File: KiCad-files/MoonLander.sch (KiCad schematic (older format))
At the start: 6 parts, among them P1 CONN_01X02, P2 CONN_01X02, P3 USB_OTG

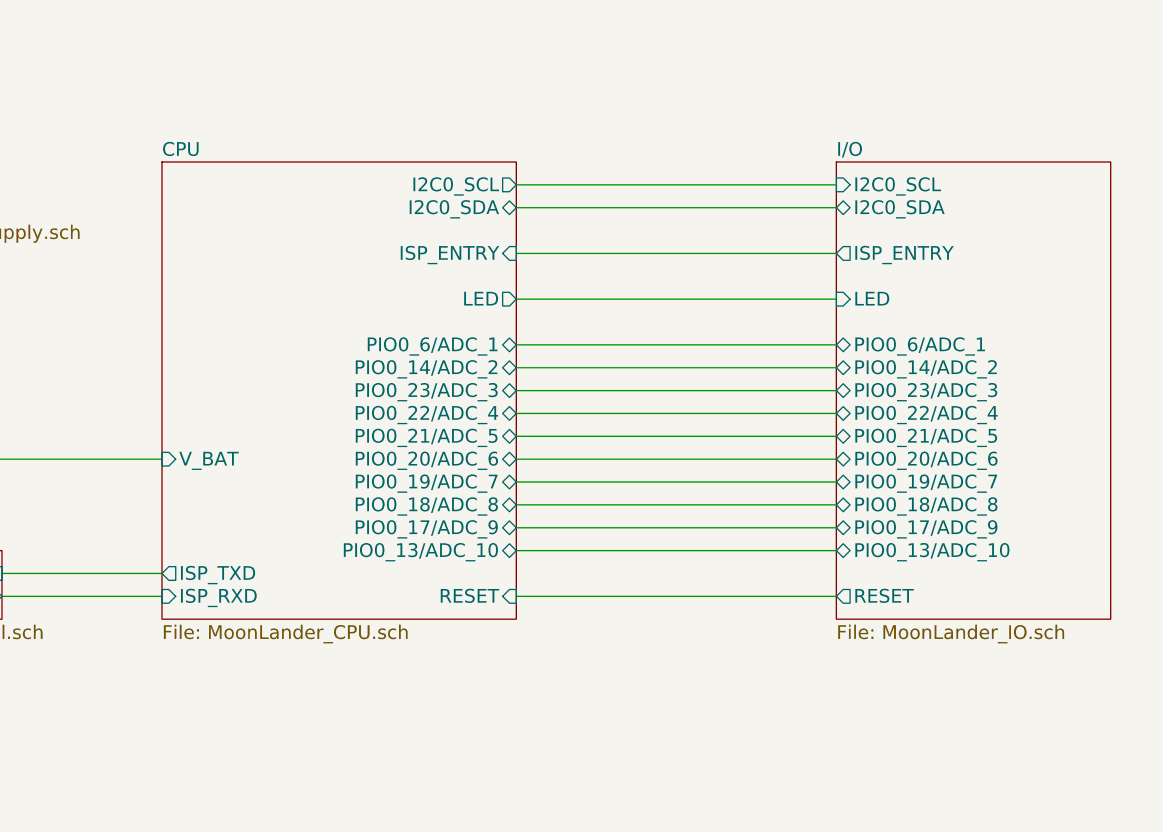
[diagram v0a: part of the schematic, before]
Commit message: added I2C EEPROM, redid ground stitching
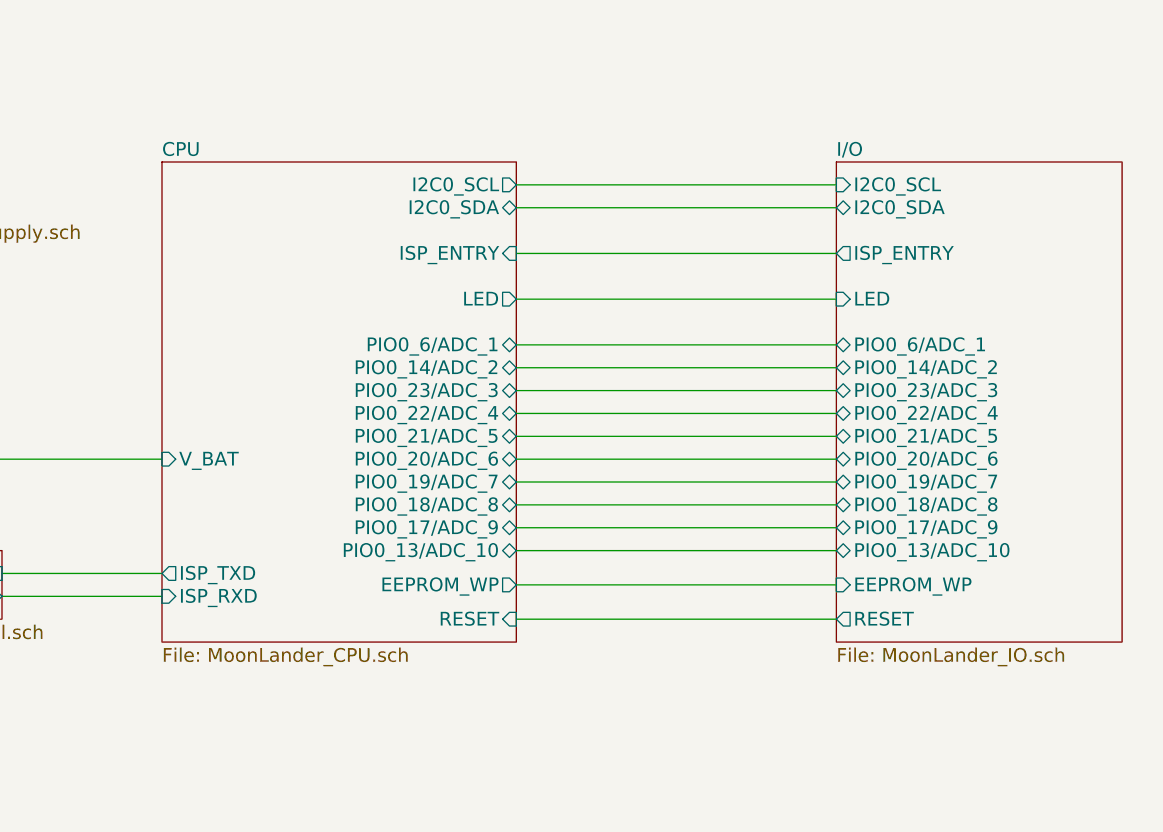
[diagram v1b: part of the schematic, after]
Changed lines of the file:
@@
 5V DC external supply
 $Sheet
-S 8450 2550 1200 2000
+S 8450 2550 1250 2100
 U 566094B7
 F0 "I/O" 60
@@
 F13 "PIO0_22/ADC_4" B L 8450 3650 60
 F14 "PIO0_23/ADC_3" B L 8450 3550 60
-F15 "RESET" O L 8450 4450 60
+F15 "RESET" O L 8450 4550 60
 F16 "LED" I L 8450 3150 60
+F17 "EEPROM_WP" I L 8450 4400 60
 $EndSheet
 Wire Wire Line
@@
 Connection ~ 3400 2700
 $Sheet
-S 5500 2550 1550 2000
+S 5500 2550 1550 2100
 U 565F2D6A
 F0 "CPU" 60
@@
 F16 "PIO0_22/ADC_4" B R 7050 3650 60
 F17 "PIO0_23/ADC_3" B R 7050 3550 60
-F18 "RESET" I R 7050 4450 60
+F18 "RESET" I R 7050 4550 60
 F19 "LED" O R 7050 3150 60
+F20 "EEPROM_WP" O R 7050 4400 60
 $EndSheet
 Wire Wire Line
@@
 	7050 4250 8450 4250
 Wire Wire Line
-	7050 4450 8450 4450
+	7050 4550 8450 4550
 Wire Wire Line
 	7050 2650 8450 2650
@@
 EndData
 $EndBitmap
+Wire Wire Line
+	7050 4400 8450 4400
 $EndSCHEMATC

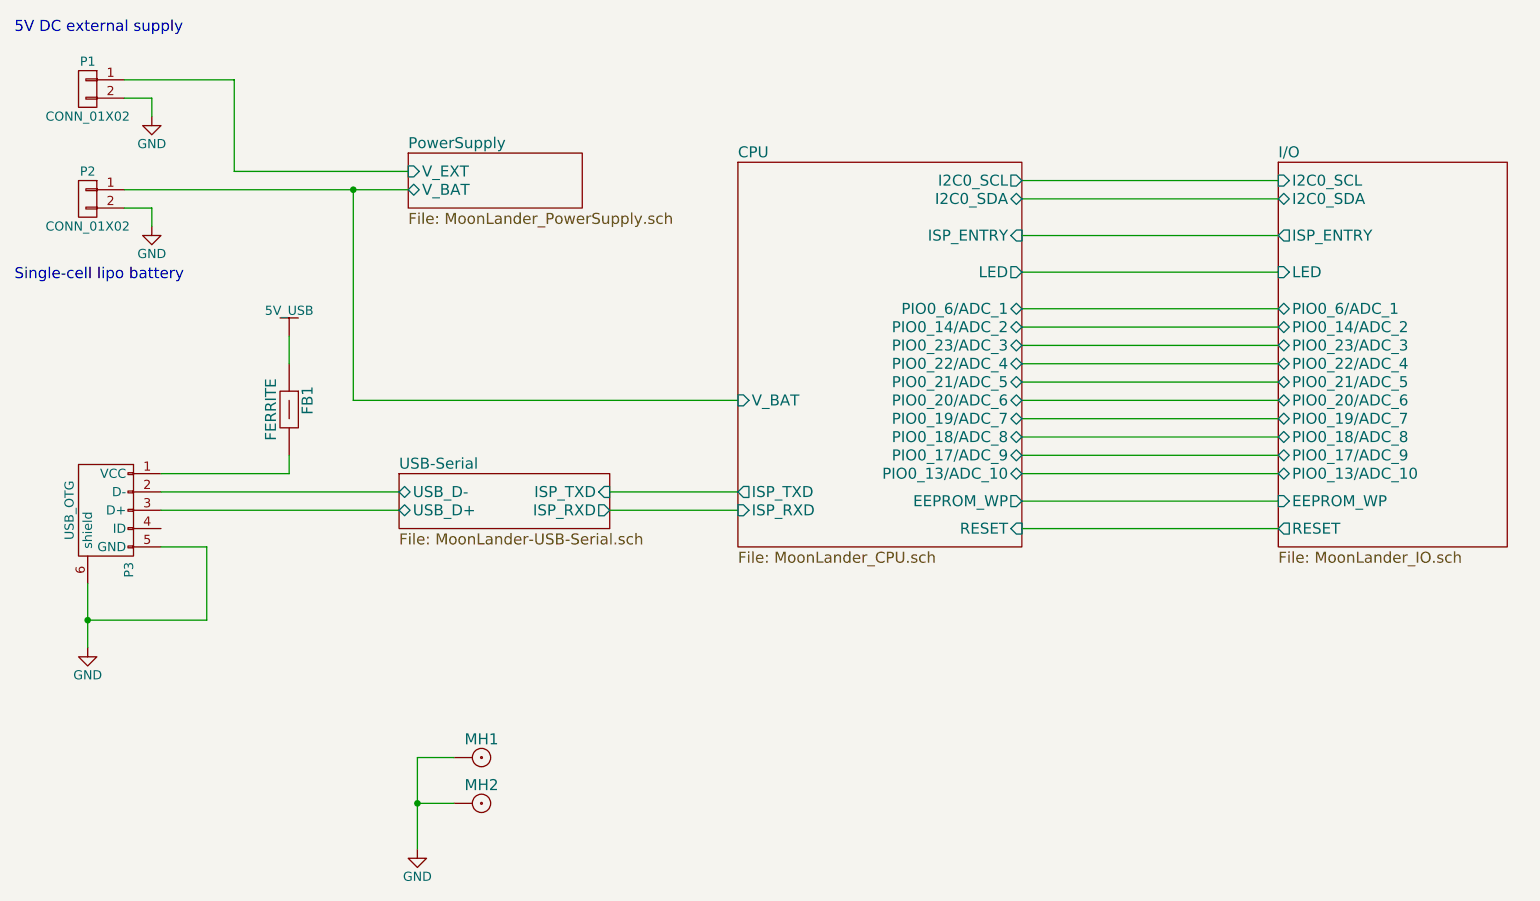
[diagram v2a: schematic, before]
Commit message: drive ISP_ENTRY and RST from CP2110 GPIO outputs
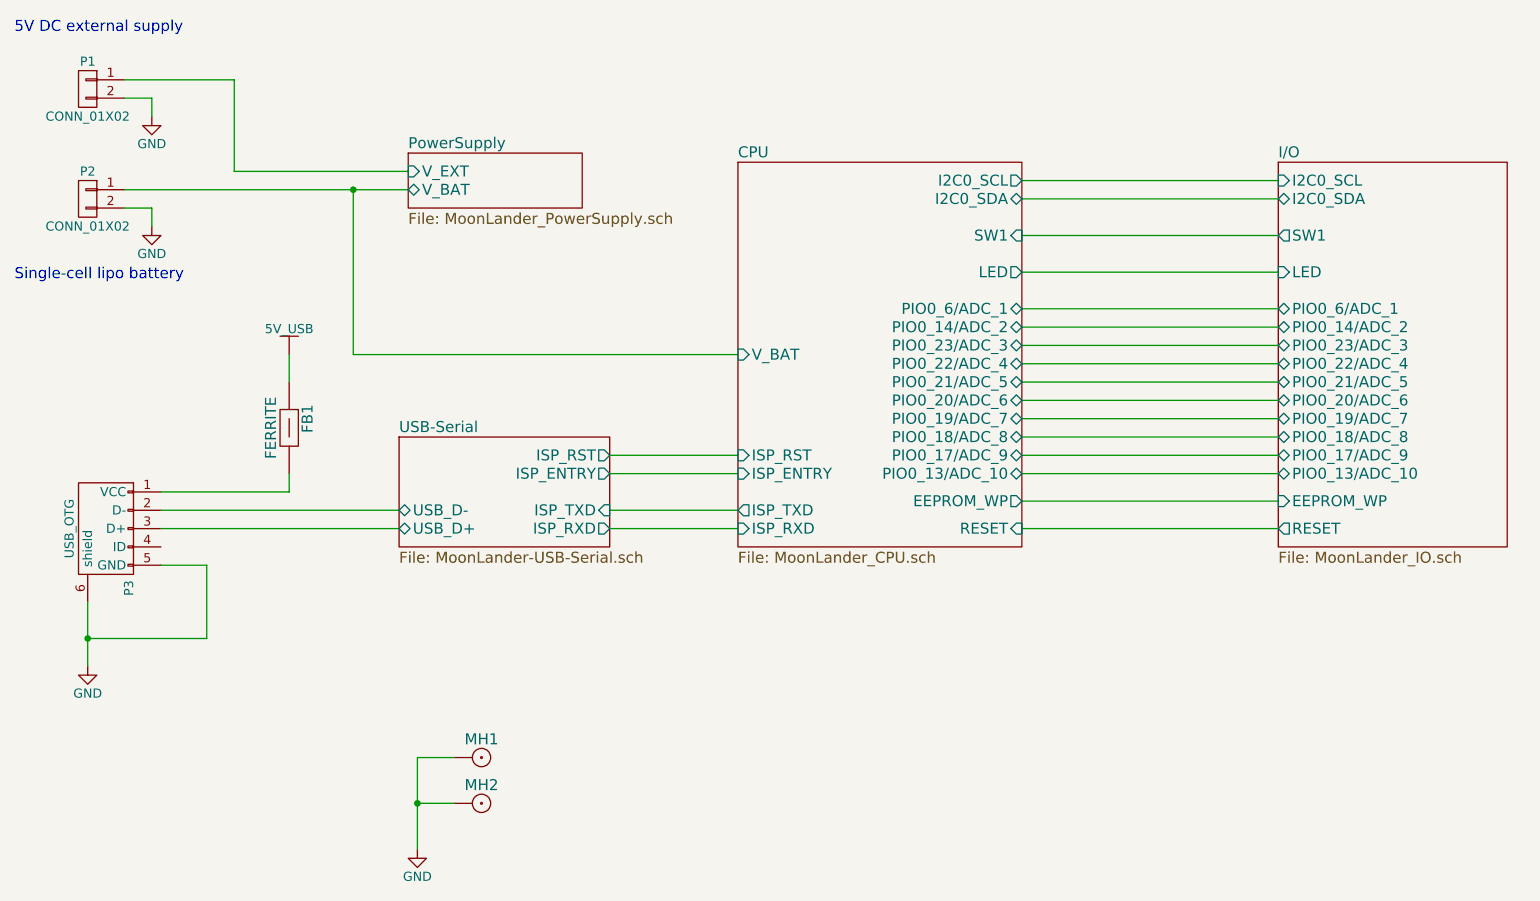
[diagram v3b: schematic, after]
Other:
- moved on the sheet: FB1, P3
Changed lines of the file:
@@
 $EndSheet
 $Sheet
-S 3650 4250 1150 300
+S 3650 4050 1150 600
 U 565F8ECE
 F0 "USB-Serial" 60
 F1 "MoonLander-USB-Serial.sch" 60
-F2 "USB_D+" B L 3650 4450 60
-F3 "USB_D-" B L 3650 4350 60
-F4 "ISP_RXD" O R 4800 4450 60
-F5 "ISP_TXD" I R 4800 4350 60
+F2 "USB_D+" B L 3650 4550 60
+F3 "USB_D-" B L 3650 4450 60
+F4 "ISP_RXD" O R 4800 4550 60
+F5 "ISP_TXD" I R 4800 4450 60
+F6 "ISP_ENTRY" O R 4800 4250 60
+F7 "ISP_RST" O R 4800 4150 60
 $EndSheet
 $Comp
 L USB_OTG P3
 U 1 1 565F8F80
-P 2050 4450
-F 0 "P3" H 2375 4325 50  0000 C CNN
-F 1 "USB_OTG" H 2050 4650 50  0000 C CNN
-F 2 "Connect:USB_Micro-B" V 2000 4350 50  0001 C CNN
-F 3 "" V 2000 4350 50  0000 C CNN
-	1    2050 4450
+P 2050 4550
+F 0 "P3" H 2375 4425 50  0000 C CNN
+F 1 "USB_OTG" H 2050 4750 50  0000 C CNN
+F 2 "Connect:USB_Micro-B" V 2000 4450 50  0001 C CNN
+F 3 "" V 2000 4450 50  0000 C CNN
+	1    2050 4550
 	0    -1   1    0
 $EndComp
@@
 L GND #PWR01
 U 1 1 565F8FC6
-P 1950 5200
-F 0 "#PWR01" H 1950 4950 50  0001 C CNN
-F 1 "GND" H 1950 5050 50  0000 C CNN
-F 2 "" H 1950 5200 50  0000 C CNN
-F 3 "" H 1950 5200 50  0000 C CNN
-	1    1950 5200
+P 1950 5300
+F 0 "#PWR01" H 1950 5050 50  0001 C CNN
+F 1 "GND" H 1950 5150 50  0000 C CNN
+F 2 "" H 1950 5300 50  0000 C CNN
+F 3 "" H 1950 5300 50  0000 C CNN
+	1    1950 5300
 	1    0    0    -1
 $EndComp
@@
 L 5V_USB #PWR02
 U 1 1 565F9205
-P 3050 3500
-F 0 "#PWR02" H 3050 3350 50  0001 C CNN
-F 1 "5V_USB" H 3050 3640 50  0000 C CNN
-F 2 "" H 3050 3500 60  0000 C CNN
-F 3 "" H 3050 3500 60  0000 C CNN
-	1    3050 3500
+P 3050 3600
+F 0 "#PWR02" H 3050 3450 50  0001 C CNN
+F 1 "5V_USB" H 3050 3740 50  0000 C CNN
+F 2 "" H 3050 3600 60  0000 C CNN
+F 3 "" H 3050 3600 60  0000 C CNN
+	1    3050 3600
 	1    0    0    -1
 $EndComp
@@
 L FERRITE FB1
 U 1 1 565F9728
-P 3050 3900
-F 0 "FB1" H 3000 4000 60  0000 C CNN
-F 1 "FERRITE" H 3050 3800 60  0000 C CNN
-F 2 "Resistors_SMD:R_0402" H 3050 3900 60  0001 C CNN
-F 3 "" H 3050 3900 60  0000 C CNN
-	1    3050 3900
+P 3050 4000
+F 0 "FB1" H 3000 4100 60  0000 C CNN
+F 1 "FERRITE" H 3050 3900 60  0000 C CNN
+F 2 "Resistors_SMD:R_0402" H 3050 4000 60  0001 C CNN
+F 3 "" H 3050 4000 60  0000 C CNN
+	1    3050 4000
 	0    1    1    0
 $EndComp
@@
 F0 "I/O" 60
 F1 "MoonLander_IO.sch" 60
-F2 "ISP_ENTRY" O L 8450 2950 60
-F3 "I2C0_SCL" I L 8450 2650 60
-F4 "I2C0_SDA" B L 8450 2750 60
-F5 "PIO0_6/ADC_1" B L 8450 3350 60
-F6 "PIO0_13/ADC_10" B L 8450 4250 60
-F7 "PIO0_14/ADC_2" B L 8450 3450 60
-F8 "PIO0_17/ADC_9" B L 8450 4150 60
-F9 "PIO0_18/ADC_8" B L 8450 4050 60
-F10 "PIO0_19/ADC_7" B L 8450 3950 60
-F11 "PIO0_20/ADC_6" B L 8450 3850 60
-F12 "PIO0_21/ADC_5" B L 8450 3750 60
-F13 "PIO0_22/ADC_4" B L 8450 3650 60
-F14 "PIO0_23/ADC_3" B L 8450 3550 60
-F15 "RESET" O L 8450 4550 60
-F16 "LED" I L 8450 3150 60
-F17 "EEPROM_WP" I L 8450 4400 60
+F2 "I2C0_SCL" I L 8450 2650 60
+F3 "I2C0_SDA" B L 8450 2750 60
+F4 "PIO0_6/ADC_1" B L 8450 3350 60
+F5 "PIO0_13/ADC_10" B L 8450 4250 60
+F6 "PIO0_14/ADC_2" B L 8450 3450 60
+F7 "PIO0_17/ADC_9" B L 8450 4150 60
+F8 "PIO0_18/ADC_8" B L 8450 4050 60
+F9 "PIO0_19/ADC_7" B L 8450 3950 60
+F10 "PIO0_20/ADC_6" B L 8450 3850 60
+F11 "PIO0_21/ADC_5" B L 8450 3750 60
+F12 "PIO0_22/ADC_4" B L 8450 3650 60
+F13 "PIO0_23/ADC_3" B L 8450 3550 60
+F14 "RESET" O L 8450 4550 60
+F15 "LED" I L 8450 3150 60
+F16 "EEPROM_WP" I L 8450 4400 60
+F17 "SW1" O L 8450 2950 60
 $EndSheet
 Wire Wire Line
-	1950 4850 1950 5200
-Wire Wire Line
-	2350 4250 3050 4250
-Wire Wire Line
-	3050 3500 3050 3650
-Wire Wire Line
-	3050 4250 3050 4150
-Wire Wire Line
-	2350 4350 3650 4350
-Wire Wire Line
-	3650 4450 2350 4450
-Wire Wire Line
-	2350 4650 2600 4650
-Wire Wire Line
-	2600 4650 2600 5050
-Wire Wire Line
-	2600 5050 1950 5050
-Connection ~ 1950 5050
+	1950 4950 1950 5300
+Wire Wire Line
+	2350 4350 3050 4350
+Wire Wire Line
+	3050 3600 3050 3750
+Wire Wire Line
+	3050 4350 3050 4250
+Wire Wire Line
+	2350 4450 3650 4450
+Wire Wire Line
+	3650 4550 2350 4550
+Wire Wire Line
+	2350 4750 2600 4750
+Wire Wire Line
+	2600 4750 2600 5150
+Wire Wire Line
+	2600 5150 1950 5150
+Connection ~ 1950 5150
 Wire Wire Line
 	2150 2700 3700 2700
@@
 	2750 2600 3700 2600
 Wire Wire Line
-	4800 4350 5500 4350
-Wire Wire Line
-	5500 4450 4800 4450
-Wire Wire Line
-	3400 2700 3400 3850
-Wire Wire Line
-	3400 3850 5500 3850
+	4800 4450 5500 4450
+Wire Wire Line
+	5500 4550 4800 4550
+Wire Wire Line
+	3400 2700 3400 3600
+Wire Wire Line
+	3400 3600 5500 3600
 Connection ~ 3400 2700
 $Sheet
@@
 F0 "CPU" 60
 F1 "MoonLander_CPU.sch" 60
-F2 "ISP_RXD" I L 5500 4450 60
-F3 "ISP_TXD" O L 5500 4350 60
+F2 "ISP_RXD" I L 5500 4550 60
+F3 "ISP_TXD" O L 5500 4450 60
 F4 "I2C0_SCL" O R 7050 2650 60
 F5 "I2C0_SDA" B R 7050 2750 60
-F6 "ISP_ENTRY" I R 7050 2950 60
-F7 "V_BAT" I L 5500 3850 60
+F6 "ISP_ENTRY" I L 5500 4250 60
+F7 "V_BAT" I L 5500 3600 60
 F8 "PIO0_6/ADC_1" B R 7050 3350 60
 F9 "PIO0_13/ADC_10" B R 7050 4250 60
@@
 F19 "LED" O R 7050 3150 60
 F20 "EEPROM_WP" O R 7050 4400 60
+F21 "SW1" I R 7050 2950 60
+F22 "ISP_RST" I L 5500 4150 60
 $EndSheet
 Wire Wire Line
@@
 03 43 83 61 8C 09 03 03 03 03 43 83 61 8C 09 03 03 03 03 43 83 61 8C 09 03 03 03 03 43 83 61 03
 60 D2 64 32 30 30 30 30 34 84 CF 1C 00 A9 00 9C 01 A8 8B 59 19 06 06 06 06 06 E9 E3 33 80 C5 FF
-07 47 25 A5 D2 E9 03 52 D8 00 00 00 00 49 45 4E 44 AE 42 60 82 00
+07 47 25 A5 D2 E9 03 52 D8 00 00 00 00 49 45 4E 44 AE 42 60 82 7F
 EndData
 $EndBitmap
 Wire Wire Line
 	7050 4400 8450 4400
+Wire Wire Line
+	5500 4150 4800 4150
+Wire Wire Line
+	4800 4250 5500 4250
 $EndSCHEMATC
